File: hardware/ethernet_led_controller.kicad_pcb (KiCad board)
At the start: 2 copper layers, 75.1 x 75 mm, 26 parts, among them J1 WeMos_CH340G_USB_to_SERIAL, J2 RJ45, J3 RJ45, J4 terminal_04, J5 terminal_04, J6 Barrel_Jack_Switch, J7 terminal_02, Q1 2N3904, Q2 2N3904, U1 WT32-ETH01, U2 74HC245

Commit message: update hardware and software
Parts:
- removed D2: LED, LED_THT:LED_D5.0mm
- added C2: 220u, Capacitor_THT:CP_Radial_D5.0mm_P2.00mm, F.Cu at (58.0, 82.0)
- added F1: Polyfuse, Fuse:Fuse_Bourns_MF-RG300, F.Cu at (57.5, 52.3)
- added J10: Conn_01x02, Connector_PinHeader_2.54mm:PinHeader_1x03_P2.54mm_Horizontal, F.Cu at (83.1, 59.5)
- added J8: MP1584EN_5v_stepdown, lib_fp:MP1584EN_stepdown_module, F.Cu at (75.8, 76.8)
- added J9: Conn_01x03, Connector_PinHeader_2.54mm:PinHeader_1x03_P2.54mm_Horizontal, F.Cu at (66.8, 59.4)
- added SW1: SW_Push, Button_Switch_THT:SW_Tactile_SKHH_Angled, F.Cu at (53.3, 127.8)
- C1: value C_Polarized_Small -> 10u
- J2, J3: footprint Connector_RJ:RJ45_Amphenol_54602-x08_Horizontal -> lib_fp:RJ45_Horizontal
- R12: value 100 -> 10k
- moved Q2 52.6 mm to (94.7, 82.3)
- moved J1 51.1 mm to (96.7, 71.8)
- moved Q1 47.0 mm to (101.7, 82.3)
- moved C1 45.9 mm to (108.0, 82.0), turned to 0 degrees
- moved R1 44.2 mm to (91.0, 75.5)
- moved R2 43.7 mm to (91.0, 84.1)
- moved R12 43.6 mm to (60.0, 129.5)
- moved R3 34.8 mm to (94.3, 127.9)
- moved R4 34.8 mm to (91.0, 127.9)
- moved R5 34.8 mm to (87.7, 127.9)
- moved R6 34.8 mm to (84.5, 127.9)
- moved R7 34.8 mm to (81.4, 127.9)
- moved R8 34.8 mm to (78.2, 127.9)
- moved U1 34.8 mm to (77.9, 100.5)
- moved U2 34.8 mm to (96.9, 117.2)
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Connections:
- J1 pad 3: unconnected-(J1-Pin_3-Pad3) -> Net-(J1-Pin_3)
- J6 pad 1: +5V -> Net-(J7-Pin_1)
- J6 pad 3: GND -> unconnected-(J6-Pad3)
- J7 pad 1: +5V -> Net-(J7-Pin_1)
- R12 pad 1: GND -> Net-(U1-IO36/ADC1_CH0/INPUT_ONLY)
- R12 pad 2: Net-(D2-K) -> +3V3
- U1 pad 10: unconnected-(U1-3.3V-Pad10) -> +3V3
- U1 pad 13: Net-(D2-A) -> unconnected-(U1-LINK_LED-Pad13)
- U1 pad 21: unconnected-(U1-IO36/ADC1_CH0/INPUT_ONLY-Pad21) -> Net-(U1-IO36/ADC1_CH0/INPUT_ONLY)
- U1 pad 3: unconnected-(U1-3.3V-Pad3) -> +3V3
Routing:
- net +3V3: track 0.00 -> 61.6 mm
- net Net-(U1-IO36/ADC1_CH0/INPUT_ONLY): track 0.00 -> 45.1 mm
- net Net-(D2-A): track 37.4 -> 0.00 mm
- net Net-(J7-Pin_1): track 0.00 -> 30.5 mm
- net GND: track 0.00 -> 29.9 mm, vias 0 -> 1
- net Net-(J4-Pin_4): track 87.7 -> 116.8 mm, vias 0 -> 1
- net Net-(J5-Pin_2): track 85.7 -> 112.9 mm, vias 0 -> 1
- net Net-(J5-Pin_4): track 80.8 -> 106.5 mm, vias 0 -> 1
- net Net-(J1-Pin_6): track 18.1 -> 42.5 mm
- net Net-(J5-Pin_3): track 83.9 -> 106.8 mm, vias 0 -> 1
- net Net-(J1-Pin_3): track 0.00 -> 22.0 mm
- net Net-(J4-Pin_3): track 100.2 -> 120.6 mm, vias 0 -> 1
- net Net-(J8-Pin_1): track 0.00 -> 17.5 mm
- net Net-(U1-IO5/BOOT_FLOAT): track 57.9 -> 41.7 mm
- net Net-(Q1-E): track 48.9 -> 33.7 mm
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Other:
- board size 75.1 x 75 mm -> 75.1 x 85 mm
- board text added: "+V"
- board text added: "5v <-> 12v"
- board text added: "CONTROLLER RESET"
- board text added: "D0-D3"
- board text added: "D3 D2 D1 D0"
- board text added: "D4-D7"
- board text added: "D7 D6 D5 D4"
- board text added: "GND"
- board text added: "GND, RTS, 5V, TX, RX, DTR"
- board text added: "LATERAL_LEDS v1_0_0 cyberboy666"
- board text added: "NETWORK CONNECTED"
- board text added: "WeMos_USB_to_SERIAL"
- board text added: "power input select"
- board text added: "power over serial"
- board text removed: "GND, RTS, --, TX, RX, DTR"
- board text removed: "ethernet_led_controller v0_2_0 cyberboy666"
- board text removed: "this needs labels on it !"

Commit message: updating hardware for v1_1_0 - change layouts etc
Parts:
- removed J10: Conn_01x02, Connector_PinHeader_2.54mm:PinHeader_1x03_P2.54mm_Horizontal
- removed J4: terminal_04, lib_fp:terminal_04
- removed J7: terminal_02, lib_fp:terminal_02
- removed J9: Conn_01x03, Connector_PinHeader_2.54mm:PinHeader_1x03_P2.54mm_Horizontal
- added C3: 0.1u, Capacitor_THT:C_Disc_D6.0mm_W2.5mm_P5.00mm, F.Cu at (147.5, 108.4)
- J5: value terminal_04 -> terminal_08; footprint lib_fp:terminal_04 -> TerminalBlock_Phoenix:TerminalBlock_Phoenix_PT-1,5-8-3.5-H_1x08_P3.50mm_Horizontal
- moved R10 110.3 mm to (176.9, 94.8), turned to 90 degrees
- moved R9 104.0 mm to (173.6, 94.7), turned to 90 degrees
- moved R8 97.7 mm to (170.1, 94.7), turned to 90 degrees
- moved R7 91.8 mm to (167.1, 94.7), turned to 90 degrees
- moved R6 86.1 mm to (164.0, 94.6), turned to 90 degrees
- moved R5 80.2 mm to (160.8, 94.7), turned to 90 degrees
- moved J3 78.0 mm to (175.0, 78.1), turned to 180 degrees
- moved R4 74.3 mm to (157.5, 94.7), turned to 90 degrees
- moved F1 72.8 mm to (93.7, 115.5), turned to 180 degrees
- moved R3 68.4 mm to (154.2, 94.7), turned to 90 degrees
- moved J6 67.9 mm to (100.8, 115.7), turned to 90 degrees
- moved C2 64.1 mm to (110.7, 118.6), turned to 90 degrees
- moved D1 55.8 mm to (88.9, 74.6)
- moved U2 55.2 mm to (151.3, 108.0), turned to 90 degrees
- moved SW1 54.7 mm to (88.6, 85.9)
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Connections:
- F1 pad 2: Net-(J9-Pin_2) -> Net-(J8-Pin_1)
- J2 pad 1: Net-(J4-Pin_1) -> Net-(J5-Pin_1)
- J2 pad 3: Net-(J4-Pin_2) -> Net-(J5-Pin_2)
- J2 pad 5: Net-(J4-Pin_3) -> Net-(J5-Pin_3)
- J2 pad 7: Net-(J4-Pin_4) -> Net-(J5-Pin_4)
- J3 pad 1: Net-(J5-Pin_1) -> Net-(J5-Pin_5)
- J3 pad 3: Net-(J5-Pin_2) -> Net-(J5-Pin_6)
- J3 pad 5: Net-(J5-Pin_3) -> Net-(J5-Pin_7)
- J3 pad 7: Net-(J5-Pin_4) -> Net-(J5-Pin_8)
- J6 pad 3: unconnected-(J6-Pad3) -> Net-(J1-Pin_3)
- R10 pad 2: Net-(J5-Pin_4) -> Net-(J5-Pin_8)
- R3 pad 2: Net-(J4-Pin_1) -> Net-(J5-Pin_1)
- R4 pad 2: Net-(J4-Pin_2) -> Net-(J5-Pin_2)
- R5 pad 2: Net-(J4-Pin_3) -> Net-(J5-Pin_3)
- R6 pad 2: Net-(J4-Pin_4) -> Net-(J5-Pin_4)
- R7 pad 2: Net-(J5-Pin_1) -> Net-(J5-Pin_5)
- R8 pad 2: Net-(J5-Pin_2) -> Net-(J5-Pin_6)
- R9 pad 2: Net-(J5-Pin_3) -> Net-(J5-Pin_7)
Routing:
- net Net-(J4-Pin_2): track 126.1 -> 0.00 mm, vias 1 -> 0
- net Net-(J4-Pin_3): track 120.6 -> 0.00 mm, vias 1 -> 0
- net Net-(J4-Pin_1): track 120.4 -> 0.00 mm, vias 1 -> 0
- net Net-(J4-Pin_4): track 116.8 -> 0.00 mm, vias 1 -> 0
- net Net-(J5-Pin_8): track 0.00 -> 78.3 mm, vias 0 -> 1
- net Net-(J5-Pin_6): track 0.00 -> 76.9 mm, vias 0 -> 1
- net Net-(J5-Pin_7): track 0.00 -> 76.0 mm, vias 0 -> 1
- net Net-(J5-Pin_5): track 0.00 -> 75.2 mm, vias 0 -> 1
- net Net-(U1-IO36/ADC1_CH0/INPUT_ONLY): track 45.1 -> 103.6 mm
- net Net-(Q1-E): track 33.7 -> 67.1 mm
- net Net-(J8-Pin_1): track 17.5 -> 50.1 mm
- net +5V: track 122.5 -> 92.3 mm, vias 0 -> 1
- net Net-(J5-Pin_2): track 112.9 -> 85.2 mm
- net Net-(F1-Pad1): track 30.5 -> 7.13 mm
- net Net-(J5-Pin_4): track 106.5 -> 83.4 mm
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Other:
- board size 75.1 x 85 mm -> 100 x 60 mm
- board text added: "D0 D1 D2 D3 D4 D5 D6 D7"
- board text added: "LATERAL_LEDS_CONTROLLER v1_1_0 cyberboy666 & __"
- board text removed: "+V"
- board text removed: "5v <-> 12v"
- board text removed: "D3 D2 D1 D0"
- board text removed: "D7 D6 D5 D4"
- board text removed: "GND"
- board text removed: "LATERAL_LEDS v1_0_0 cyberboy666"
- board text removed: "power input select"
- board text removed: "power over serial"

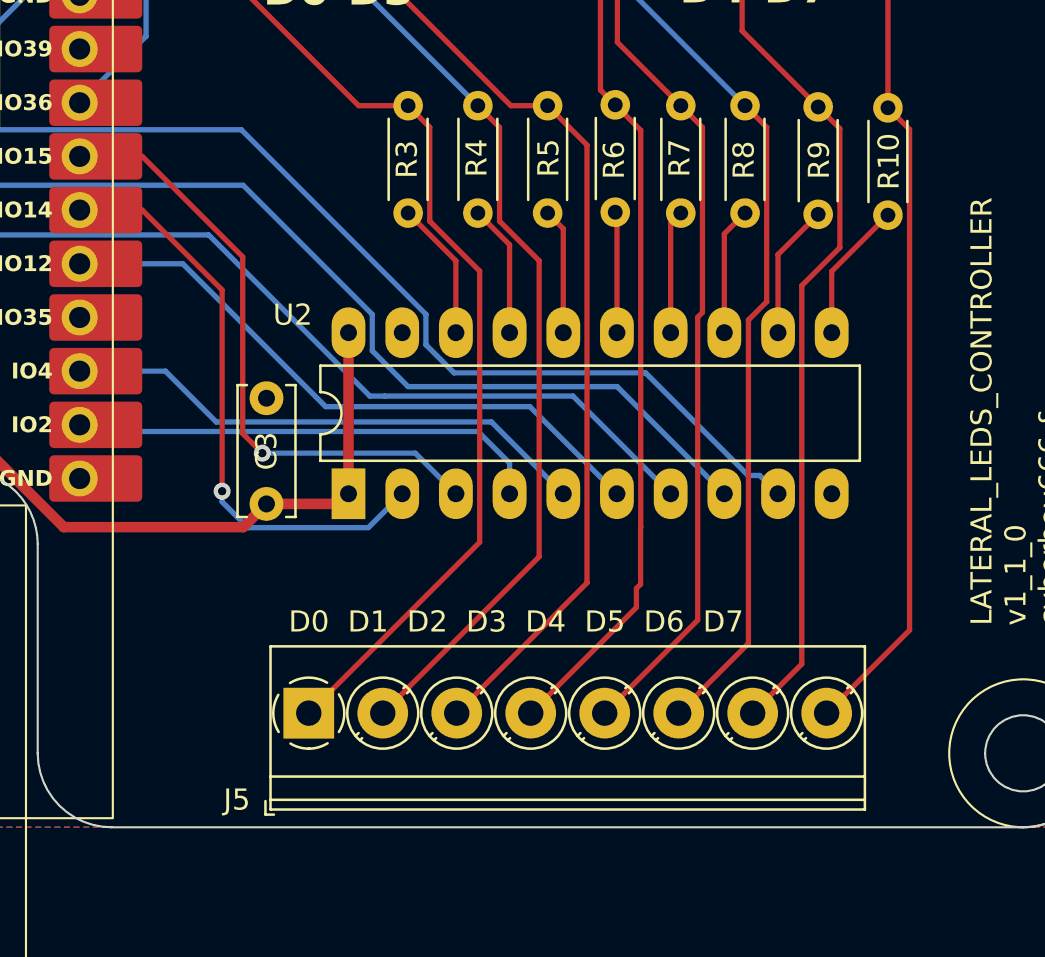
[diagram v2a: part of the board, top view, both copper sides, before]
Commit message: updated board to use 4x terminal blocks
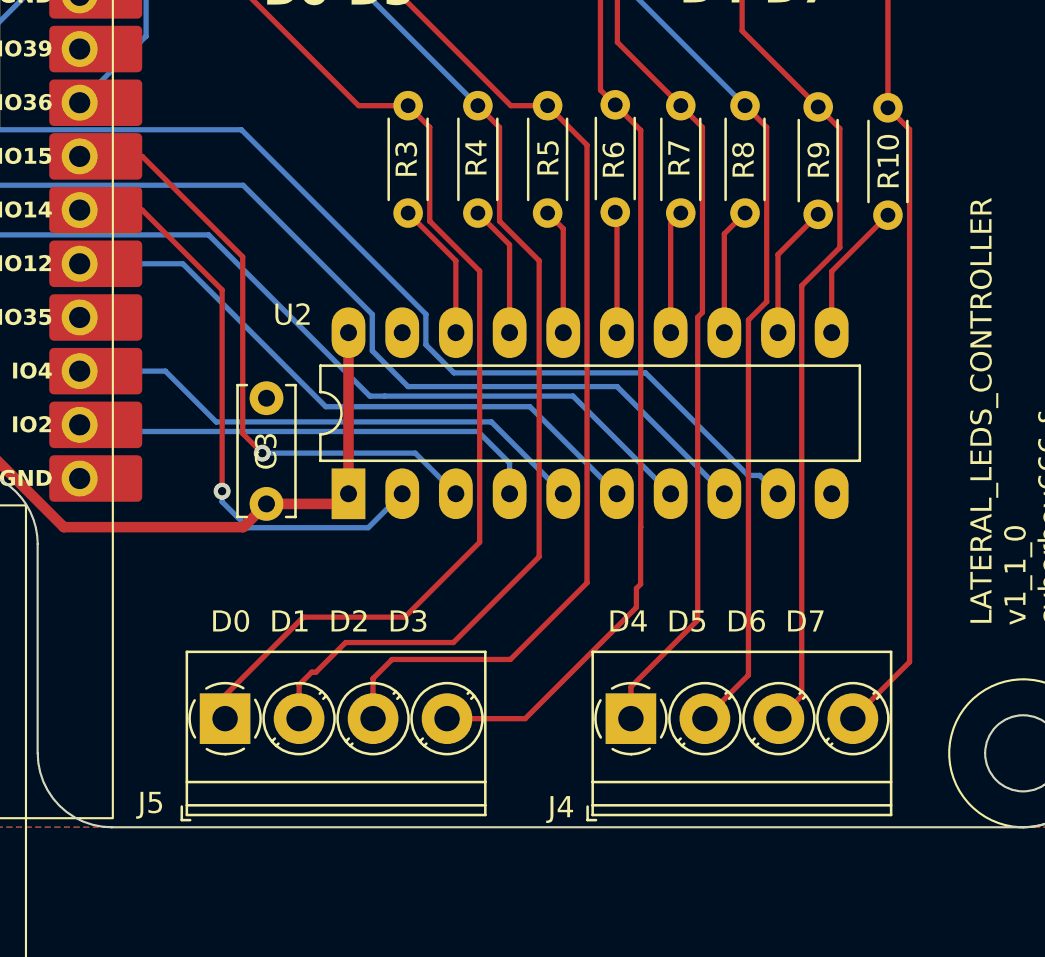
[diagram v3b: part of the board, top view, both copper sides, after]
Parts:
- added J4: terminal_04, TerminalBlock_Phoenix:TerminalBlock_Phoenix_PT-1,5-4-3.5-H_1x04_P3.50mm_Horizontal, F.Cu at (164.7, 118.6)
- J5: value terminal_08 -> terminal_04; footprint TerminalBlock_Phoenix:TerminalBlock_Phoenix_PT-1,5-8-3.5-H_1x08_P3.50mm_Horizontal -> TerminalBlock_Phoenix:TerminalBlock_Phoenix_PT-1,5-4-3.5-H_1x04_P3.50mm_Horizontal
- moved J5 3.97 mm to (145.5, 118.6)
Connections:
- J3 pad 1: Net-(J5-Pin_5) -> Net-(J4-Pin_1)
- J3 pad 3: Net-(J5-Pin_6) -> Net-(J4-Pin_2)
- J3 pad 5: Net-(J5-Pin_7) -> Net-(J4-Pin_3)
- J3 pad 7: Net-(J5-Pin_8) -> Net-(J4-Pin_4)
- R10 pad 2: Net-(J5-Pin_8) -> Net-(J4-Pin_4)
- R7 pad 2: Net-(J5-Pin_5) -> Net-(J4-Pin_1)
- R8 pad 2: Net-(J5-Pin_6) -> Net-(J4-Pin_2)
- R9 pad 2: Net-(J5-Pin_7) -> Net-(J4-Pin_3)
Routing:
- net Net-(J5-Pin_8): track 78.3 -> 0.00 mm, vias 1 -> 0
- net Net-(J4-Pin_4): track 0.00 -> 78.1 mm, vias 0 -> 1
- net Net-(J5-Pin_6): track 76.9 -> 0.00 mm, vias 1 -> 0
- net Net-(J4-Pin_2): track 0.00 -> 76.6 mm, vias 0 -> 1
- net Net-(J5-Pin_7): track 76.0 -> 0.00 mm, vias 1 -> 0
- net Net-(J4-Pin_3): track 0.00 -> 75.8 mm, vias 0 -> 1
- net Net-(J5-Pin_5): track 75.2 -> 0.00 mm, vias 1 -> 0
- net Net-(J4-Pin_1): track 0.00 -> 75.0 mm, vias 0 -> 1
- net Net-(J5-Pin_3): track 84.1 -> 89.3 mm
- net Net-(J5-Pin_2): track 85.2 -> 90.2 mm
- net Net-(J5-Pin_1): track 81.1 -> 85.8 mm
- net Net-(J5-Pin_4): track 83.4 -> 87.4 mm
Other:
- board text added: "D0 D1 D2 D3"
- board text added: "D4 D5 D6 D7"
- board text removed: "D0 D1 D2 D3 D4 D5 D6 D7"

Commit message: update hardware to v1_1_0
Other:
- board text added: "LATERAL_LEDS_CONTROLLER v1_1_0 cyberboy666 & tor"
- board text removed: "LATERAL_LEDS_CONTROLLER v1_1_0 cyberboy666 & __"
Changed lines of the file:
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@@
       (drillshape 0)
       (scaleselection 1)
-      (outputdirectory "ethernet_led_controller_v1_0_0")
+      (outputdirectory "ethernet_led_controller_v1_1_0")
     )
   )
@@
     (effects (font (size 1 1) (thickness 0.15)) (justify left bottom))
   )
-  (gr_text "LATERAL_LEDS_CONTROLLER\nv1_1_0\ncyberboy666 & __" (at 185.1 114.2 90) (layer "F.SilkS")
+  (gr_text "LATERAL_LEDS_CONTROLLER\nv1_1_0\ncyberboy666 & tor" (at 185.1 114.2 90) (layer "F.SilkS")
     (effects (font (size 1 1) (thickness 0.15)) (justify left bottom))
   )

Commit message: update hardware to v1_2_0
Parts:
- added D2: 1n5819, Diode_THT:D_DO-34_SOD68_P7.62mm_Horizontal, F.Cu at (105.0, 113.7)
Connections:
- J1 pad 3: Net-(J1-Pin_3) -> Net-(D2-A)
- J6 pad 3: Net-(J1-Pin_3) -> unconnected-(J6-Pad3)
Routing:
- net Net-(J1-Pin_3): track 15.0 -> 0.00 mm
- net Net-(D2-A): track 0.00 -> 10.00 mm
- net +5V: track 92.3 -> 101.3 mm
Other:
- board text added: "LATERAL_LED_CONTROLLER v1_2_0 cyberboy666 & tor"
- board text removed: "LATERAL_LEDS_CONTROLLER v1_1_0 cyberboy666 & tor"
